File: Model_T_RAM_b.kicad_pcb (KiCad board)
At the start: 2 copper layers, 19.8 x 34.3 mm, 4 parts, among them J1 KC-85_RAM, U1 6264, U2 74HC86

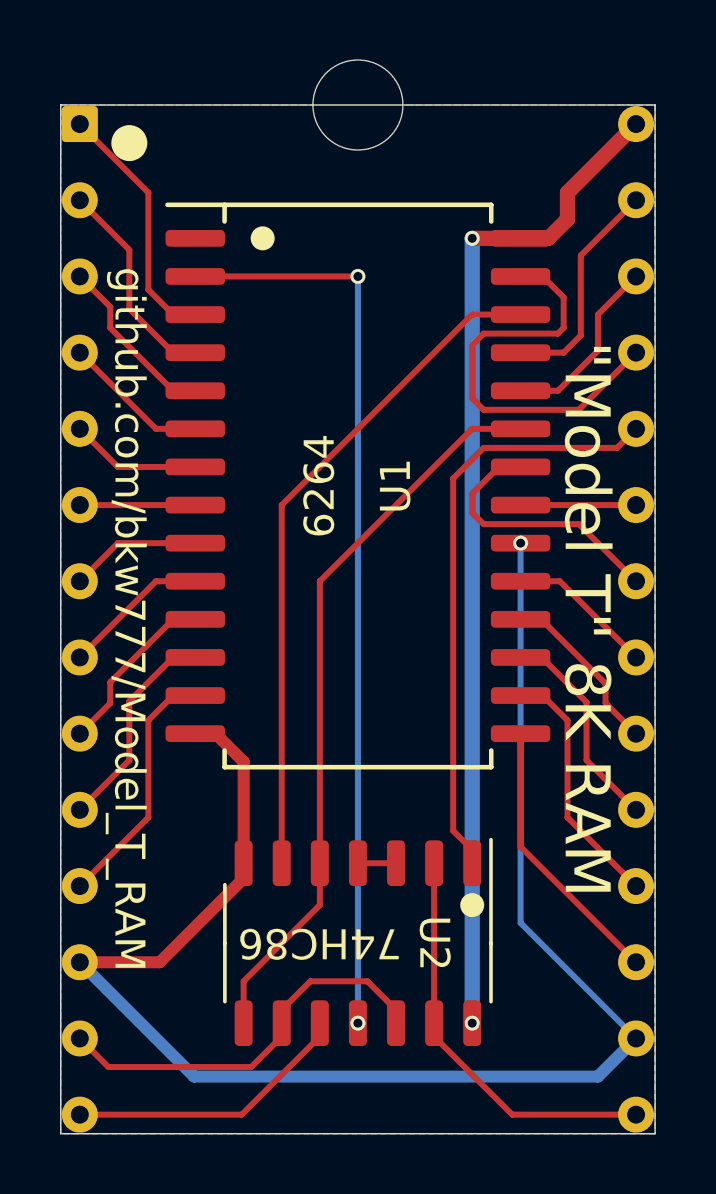
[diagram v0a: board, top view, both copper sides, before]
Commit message: v002 fewer vias
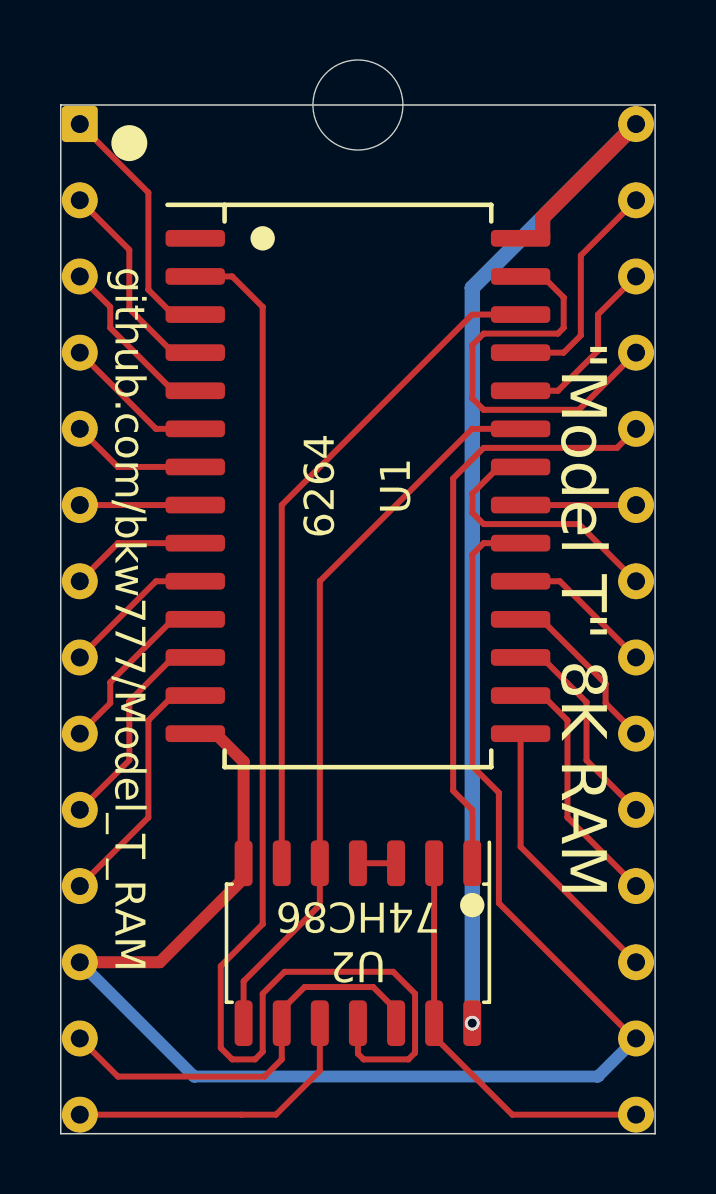
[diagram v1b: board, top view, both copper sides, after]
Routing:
- net /A12: track 30.3 -> 42.3 mm, vias 2 -> 0
- net VCC: track 33.7 -> 37.3 mm, vias 2 -> 1
- net GND: track 51.3 -> 53.4 mm, vias 1 -> 0
- net /~CS_B: track 9.53 -> 10.2 mm
- net /~CS_A: track 13.5 -> 14.0 mm
- removed copper zone on B.Cu, net GND
- removed copper zone on F.Cu, net GND
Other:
- board text added: "v002"

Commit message: tiny tidying
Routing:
- net GND: track 53.4 -> 52.1 mm
- net /AD3: track 9.21 -> 9.72 mm
